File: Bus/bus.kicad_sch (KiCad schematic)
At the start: 0 parts

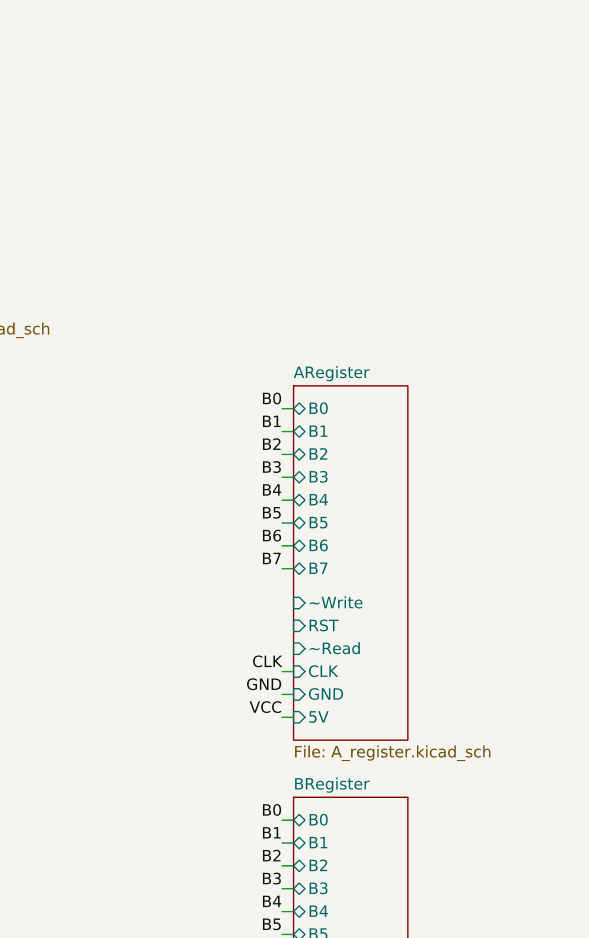
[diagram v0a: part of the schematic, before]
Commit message: Added the ALU to the bus schematic
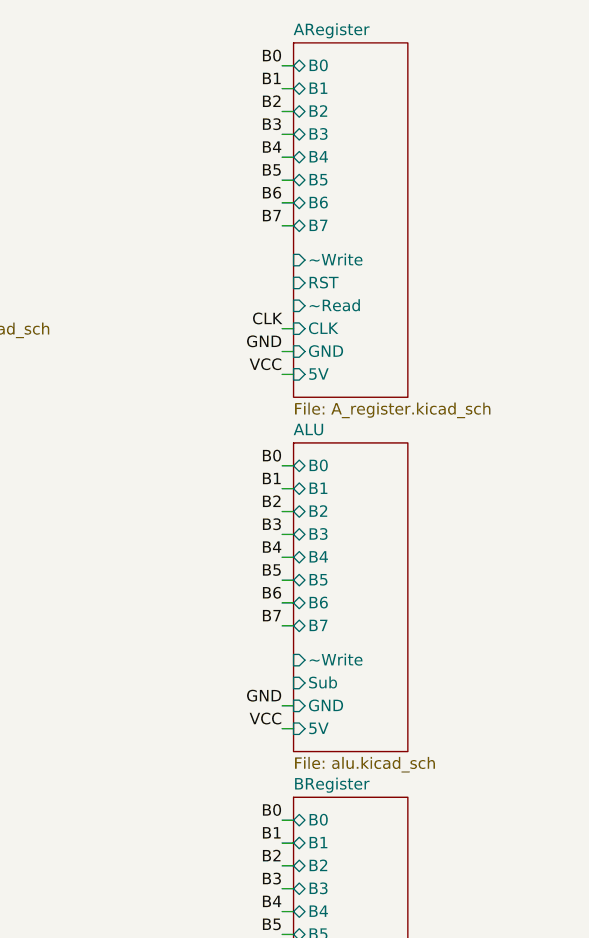
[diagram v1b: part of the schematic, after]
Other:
- added sheet ALU (alu.kicad_sch)

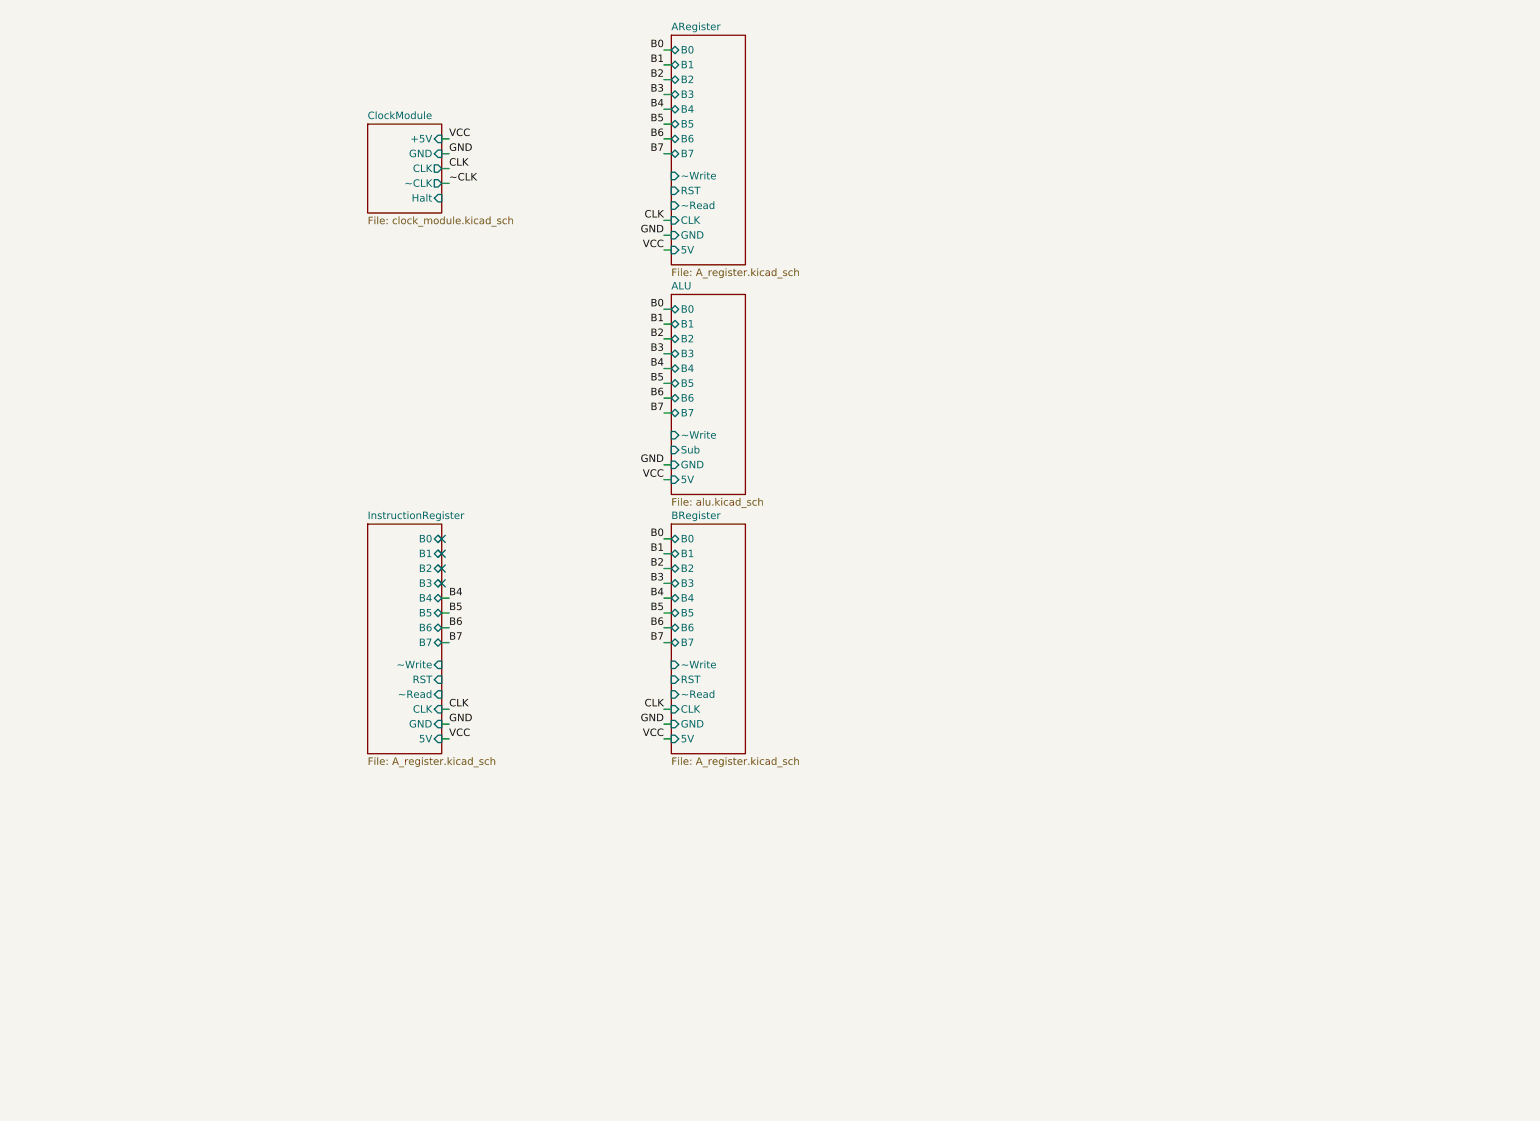
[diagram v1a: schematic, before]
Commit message: Some initial bus layout
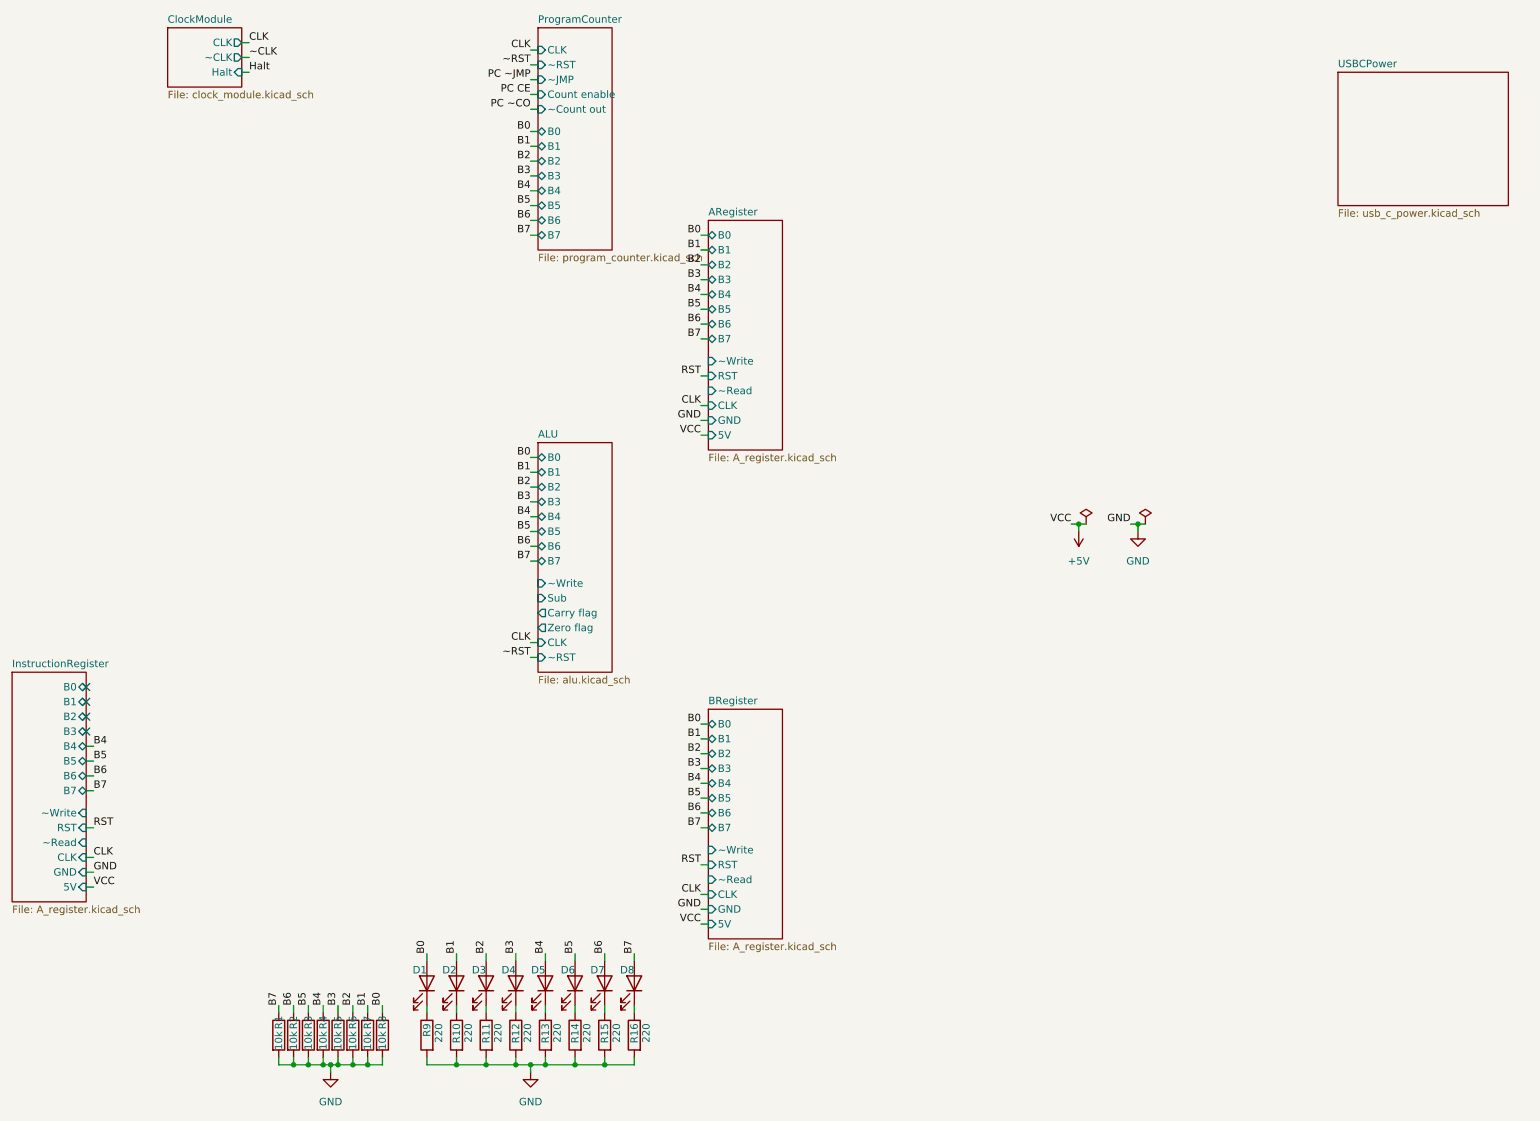
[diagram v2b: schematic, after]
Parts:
- added D1, D2, D3, D4, D5, D6, D7, D8: LED, LED_THT:LED_D5.0mm, symbol Device:LED
- added R1, R2, R3, R4, R5, R6, R7, R8: 10k, _DownloadFootprints:CF_series_Resistors_THT, symbol Device:R
- added R10, R11, R12, R13, R14, R15, R16, R9: 220, _DownloadFootprints:CF_series_Resistors_THT, symbol Device:R
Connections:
- net B0: now also D1.2 (A), R8.1
- net B1: now also D2.2 (A), R7.1
- net B2: now also D3.2 (A), R6.1
- net B3: now also D4.2 (A), R5.1
- net B4: now also D5.2 (A), R4.1
- net B5: now also D6.2 (A), R3.1
- net B6: now also D7.2 (A), R2.1
- net B7: now also D8.2 (A), R1.1
- net GND: now also R1.2, R10.2, R11.2, R12.2, R13.2, R14.2, R15.2, R16.2, R2.2, R3.2, R4.2, R5.2, R6.2, R7.2, R8.2, R9.2
- new net: D8.1 (K), R16.1
- new net: D5.1 (K), R13.1
- new net: D2.1 (K), R10.1
- new net: D3.1 (K), R11.1
- new net: D6.1 (K), R14.1
- new net: D4.1 (K), R12.1
- new net: D7.1 (K), R15.1
- new net: D1.1 (K), R9.1
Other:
- added sheet ProgramCounter (program_counter.kicad_sch)
- added sheet USBCPower (usb_c_power.kicad_sch)
- sheet ALU ports: added CLK, Carry flag, Zero flag, ~RST; removed 5V, GND
- sheet ClockModule ports: added none; removed +5V, GND

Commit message: Updated bus schematics with pinout of MAR/ALU/Registers on PCBs ordered
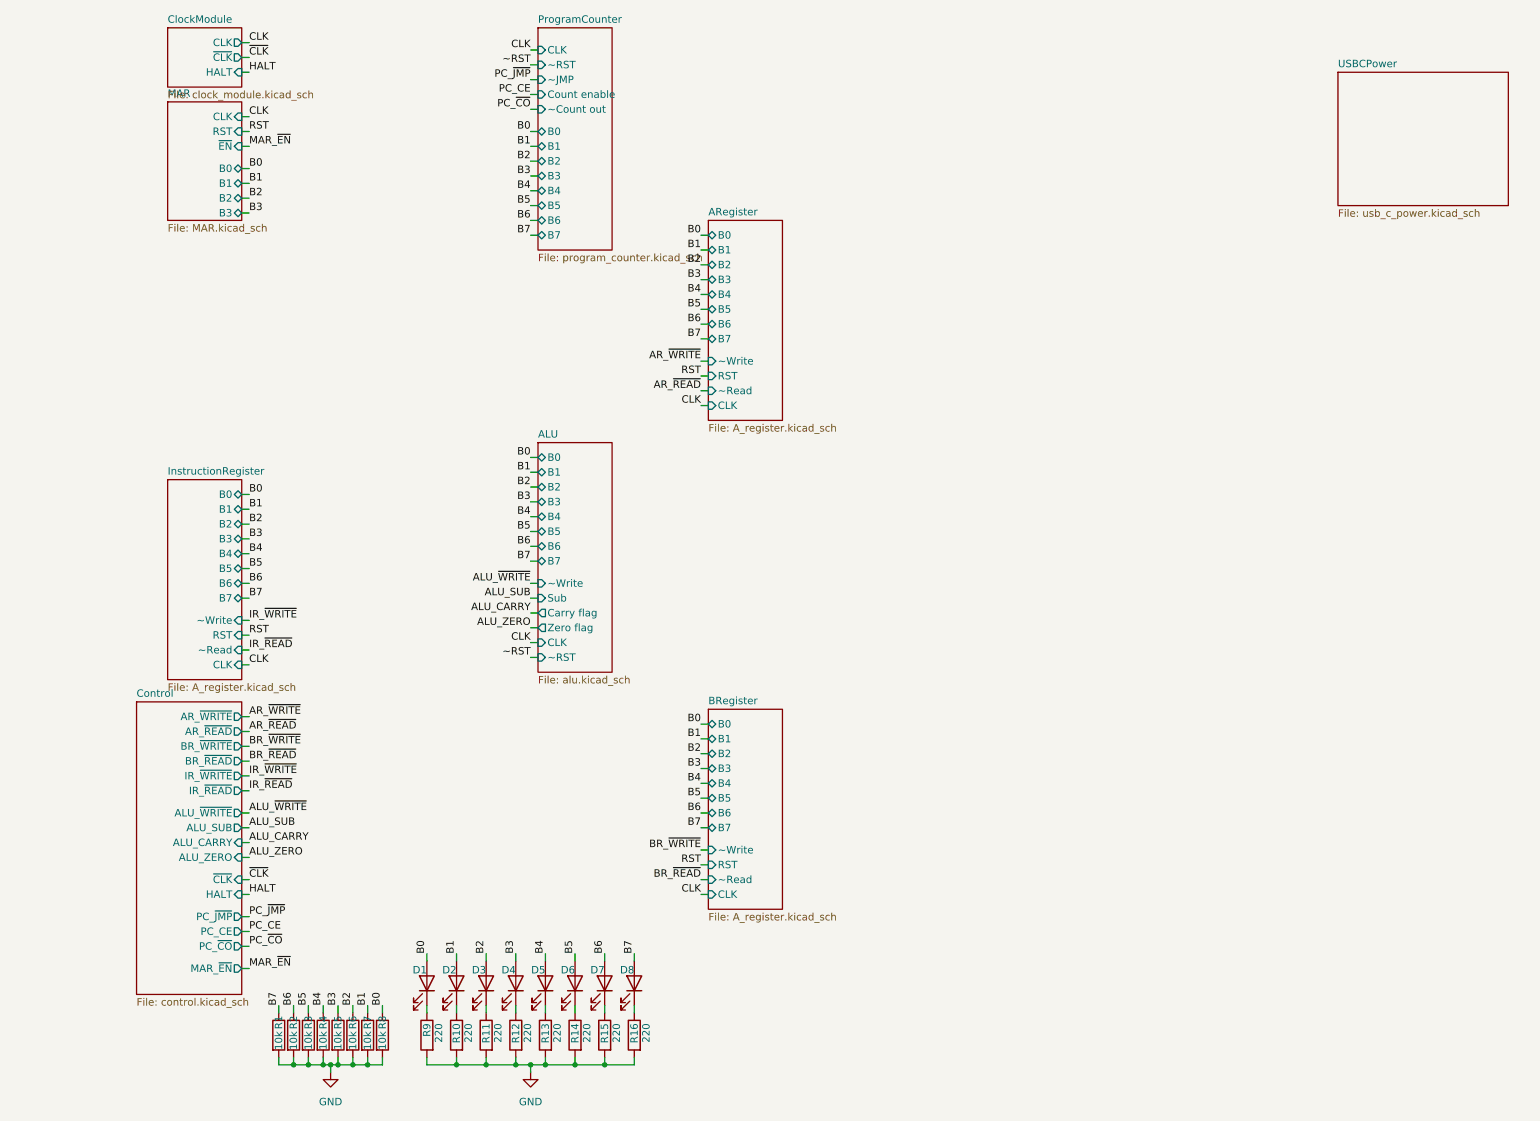
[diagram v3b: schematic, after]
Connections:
- no-connect marks 4 -> 0
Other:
- added sheet Control (control.kicad_sch)
- added sheet MAR (MAR.kicad_sch)
- sheet ARegister ports: added none; removed 5V, GND
- sheet BRegister ports: added none; removed 5V, GND
- sheet ClockModule ports: added HALT, ~{CLK}; removed Halt, ~CLK
- sheet InstructionRegister ports: added none; removed 5V, GND

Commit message: Updated bus schematic control pins and added spare bus connection
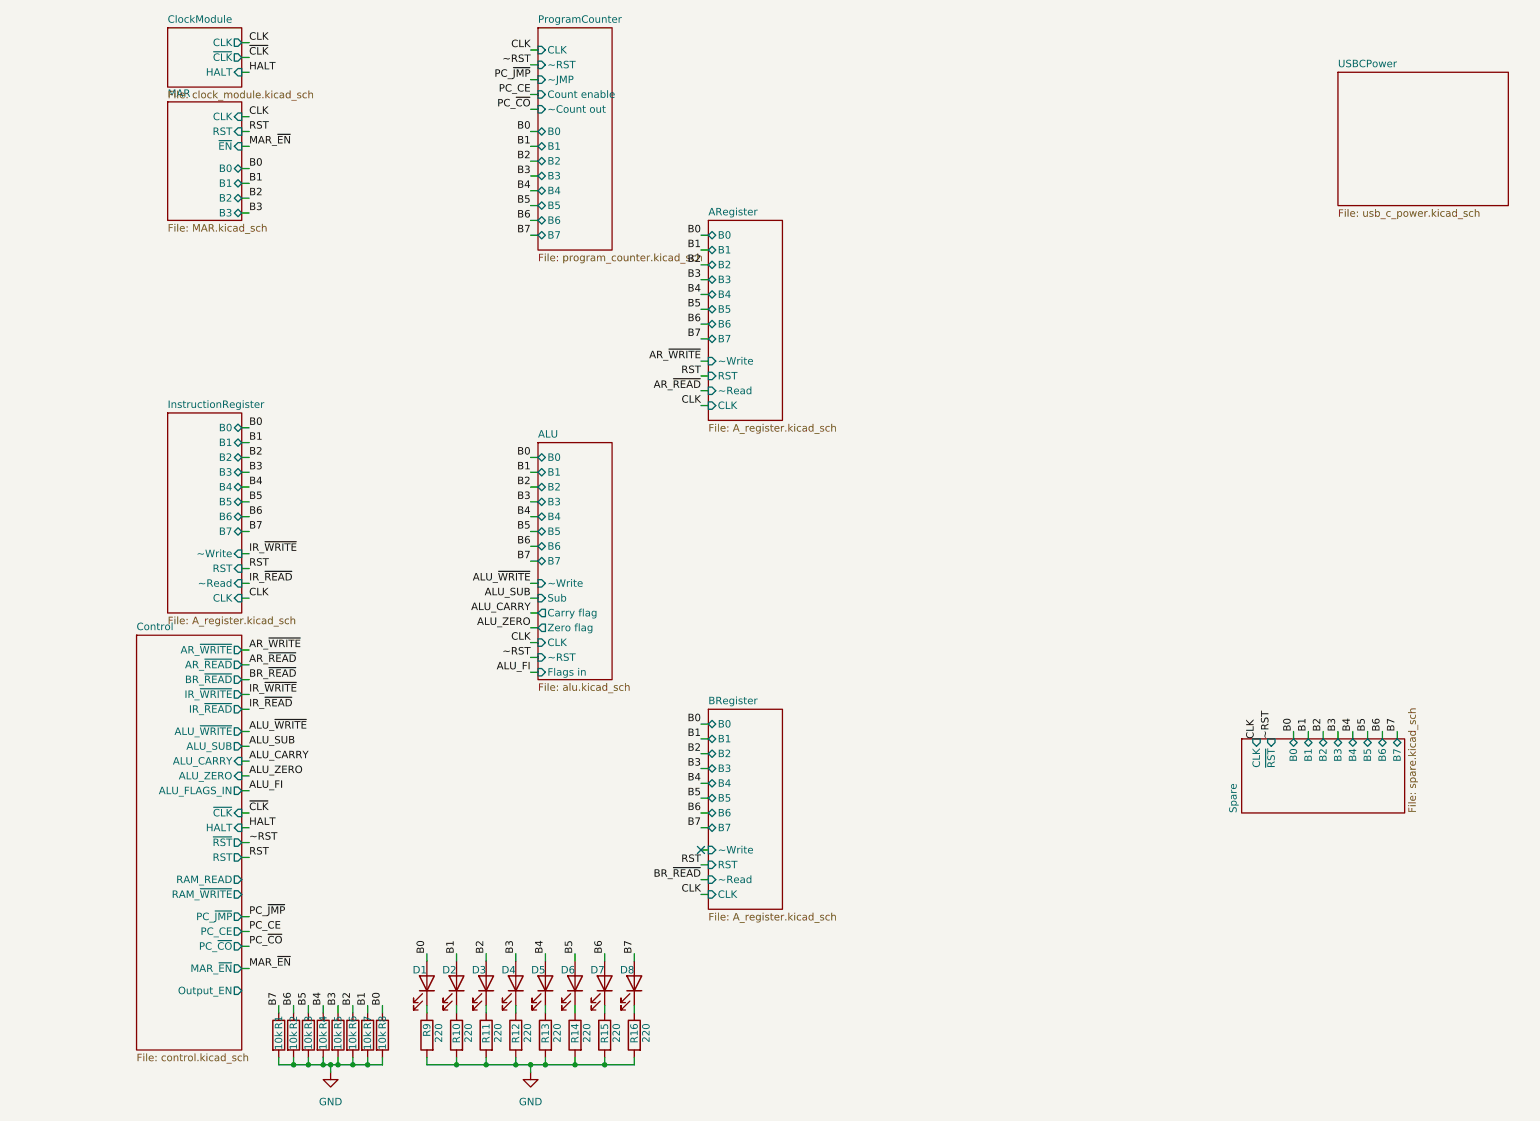
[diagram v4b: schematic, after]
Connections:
- no-connect marks 0 -> 1
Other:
- added sheet Spare (spare.kicad_sch)
- sheet ALU ports: added Flags in; removed none
- sheet Control ports: added ALU_FLAGS_IN, Output_EN, RAM_READ, RAM_~{WRITE}, RST, ~{RST}; removed BR_~{WRITE}

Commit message: Added RAM to bus
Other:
- added sheet RAM (ram.kicad_sch)

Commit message: Updated bus schmatic pins to match final layouts
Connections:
- no-connect marks 1 -> 2
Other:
- added sheet Output (output.kicad_sch)
- sheet InstructionRegister: file A_register.kicad_sch -> instruction_register.kicad_sch

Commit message: Output enable should be active low so I updated control to pass it through an inverter
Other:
- sheet Control ports: added Output_~{EN}; removed Output_EN
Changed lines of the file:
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@@
 		)
 	)
-	(label "Output_EN"
+	(label "Output_~{EN}"
 		(at 158.75 161.29 0)
 		(fields_autoplaced yes)
@@
 		)
 	)
-	(label "Output_EN"
+	(label "Output_~{EN}"
 		(at 60.96 180.34 0)
 		(fields_autoplaced yes)
@@
 			)
 		)
-		(pin "Output_EN" output
-			(at 59.69 180.34 0)
-			(effects
-				(font
-					(size 1.27 1.27)
-				)
-				(justify right)
-			)
-		)
 		(pin "RAM_~{WRITE}" output
 			(at 59.69 163.83 0)
@@
 			(effects
 				(font
+					(size 1.27 1.27)
+				)
+				(justify right)
+			)
+		)
+		(pin "Output_~{EN}" output
+			(at 59.69 180.34 0)
+			(effects
+				(font

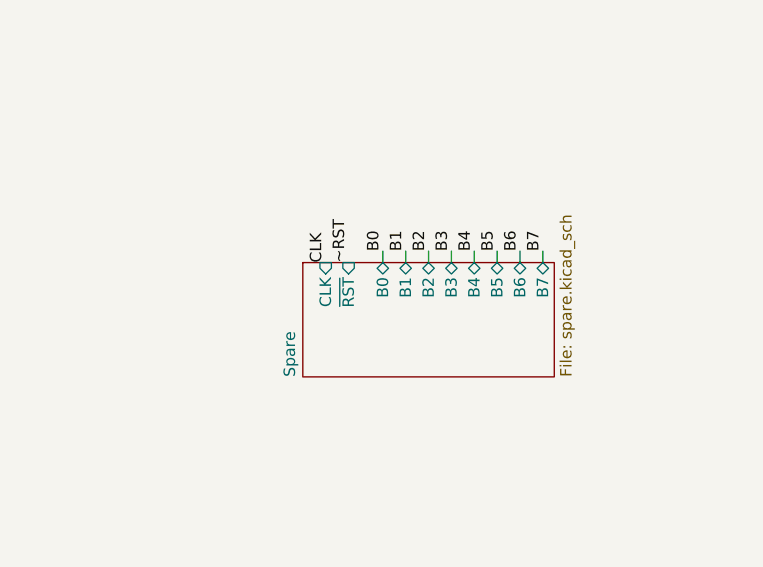
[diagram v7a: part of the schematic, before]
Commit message: Added ~clk to the spare signals
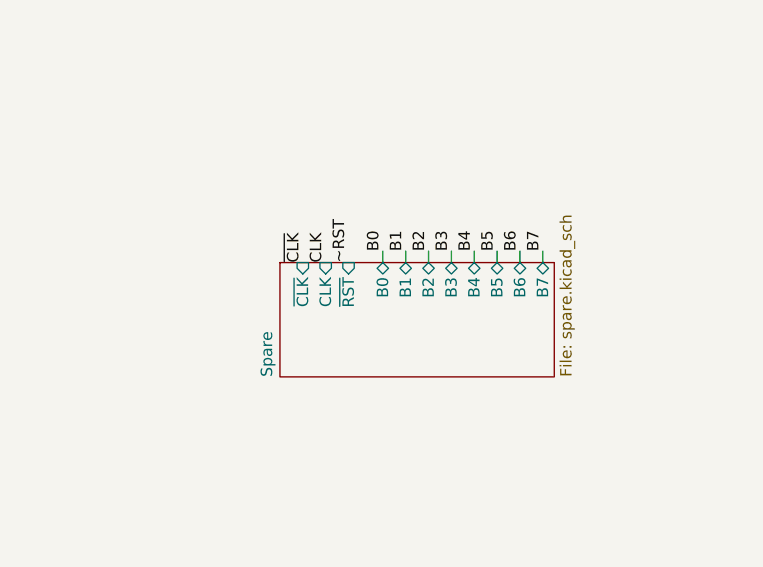
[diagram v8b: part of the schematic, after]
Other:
- sheet Spare ports: added ~{CLK}; removed none
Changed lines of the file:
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@@
+		)
+	)
+	(label "~{CLK}"
+		(at 231.14 137.16 90)
+		(fields_autoplaced yes)
+		(effects
+			(font
+				(size 1.27 1.27)
+			)
+			(justify left bottom)
 		)
 	)
@@
 	)
 	(sheet
-		(at 231.14 137.16)
-		(size 27.94 12.7)
+		(at 228.6 137.16)
+		(size 30.48 12.7)
 		(fields_autoplaced yes)
 		(stroke
@@
 		)
 		(property "Sheetname" "Spare"
-			(at 230.4284 149.86 90)
+			(at 227.8884 149.86 90)
 			(effects
 				(font
@@
 			(effects
 				(font
+					(size 1.27 1.27)
+				)
+				(justify right)
+			)
+		)
+		(pin "~{CLK}" input
+			(at 231.14 137.16 90)
+			(effects
+				(font
